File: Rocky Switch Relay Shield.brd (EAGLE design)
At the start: 69.7 x 47.6 mm, 20 parts

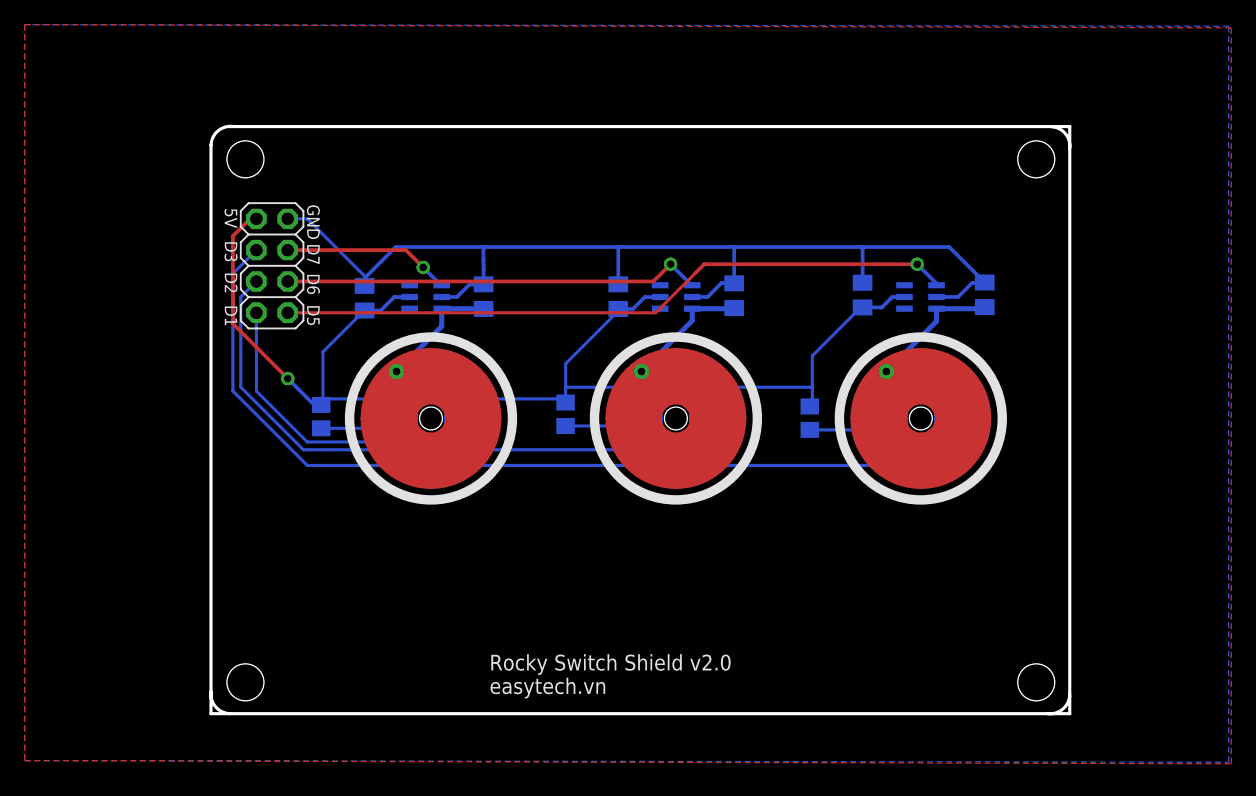
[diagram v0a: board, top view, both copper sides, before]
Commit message: Update shield relay to move touch ICs to the left
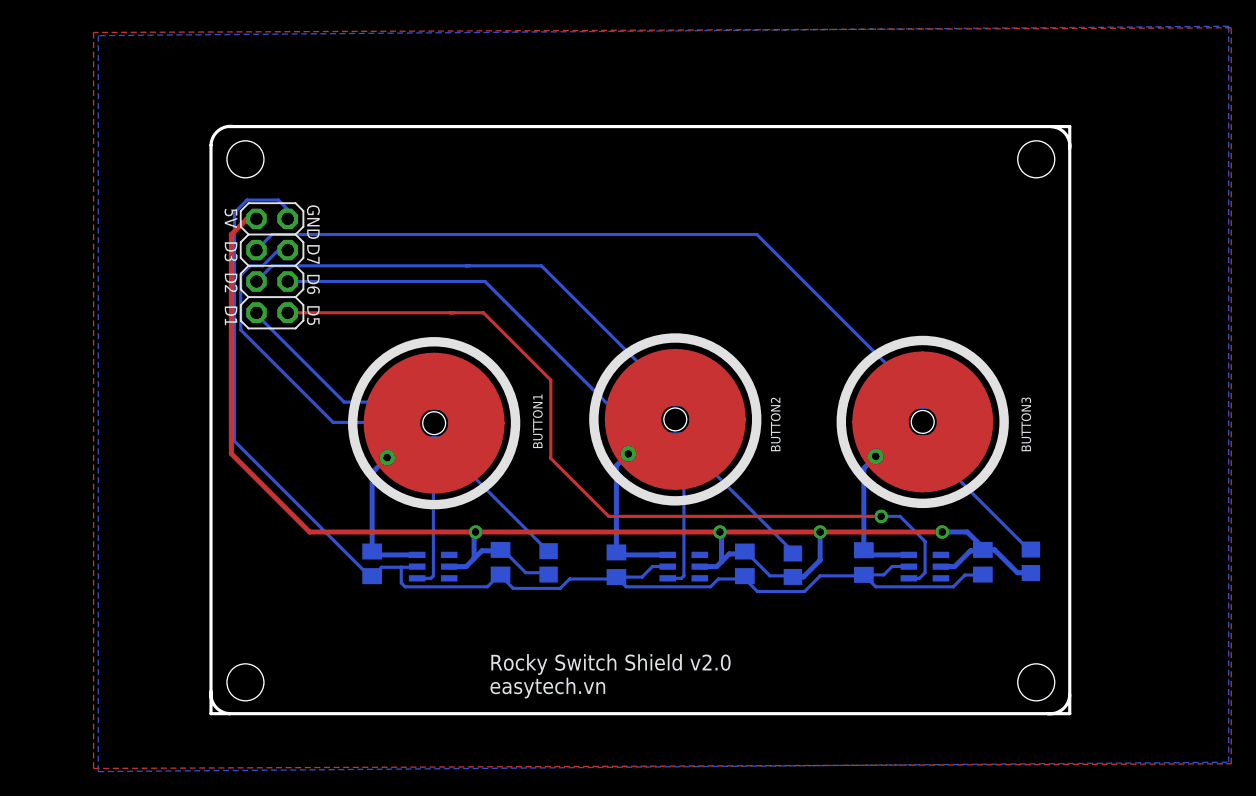
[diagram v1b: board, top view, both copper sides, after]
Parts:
- moved C2 24.1 mm to (26.1, 16.6), turned to 270 degrees
- moved C4 24.0 mm to (46.0, 16.5), turned to 270 degrees
- moved C5 23.8 mm to (55.6, 16.6), turned to 270 degrees
- moved C3 23.8 mm to (35.5, 16.4), turned to 270 degrees
- moved C6 23.8 mm to (65.3, 16.6), turned to 270 degrees
- moved C1 23.5 mm to (15.7, 16.5), turned to 270 degrees
- moved R2 22.1 mm to (49.9, 16.4), turned to 90 degrees
- moved R1 21.9 mm to (30.0, 16.5), turned to 90 degrees
- moved U$16 21.9 mm to (20.7, 16.2), turned to 270 degrees
- moved U$18 21.9 mm to (41.0, 16.2), turned to 270 degrees
- moved U$19 21.9 mm to (60.6, 16.2), turned to 270 degrees
- moved R3 21.4 mm to (69.2, 16.7), turned to 90 degrees
- moved BUTTON1 0.46 mm to (20.8, 27.9), turned to 90 degrees
- moved BUTTON3 0.32 mm to (60.4, 28.0), turned to 90 degrees
- moved BUTTON2 0.09 mm to (40.3, 28.2), turned to 90 degrees
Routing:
- net D7: track 13.8 -> 39.2 mm, vias 1 -> 0
- net 5V: track 99.7 -> 122.2 mm, vias 1 -> 4
- net GND: track 85.4 -> 105.6 mm
- net D6: track 34.1 -> 48.0 mm, vias 1 -> 0
- net D3: track 74.2 -> 60.4 mm
- net D5: track 55.3 -> 67.4 mm
- net D2: track 49.8 -> 39.2 mm
- net D1: track 25.1 -> 17.7 mm
- net N$15: track 7.74 -> 13.4 mm
- net N$10: track 7.69 -> 12.9 mm
- net N$16: track 7.84 -> 12.6 mm
- net I2: track 10.2 -> 12.6 mm
- net I1: track 10.0 -> 11.9 mm
- net I3: track 10.7 -> 11.8 mm
